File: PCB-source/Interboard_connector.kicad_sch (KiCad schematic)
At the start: 1 part, among them J1 86093488324755V1LF

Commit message: ch32
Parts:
- added J4: Conn_01x16_Socket, Connector_PinSocket_2.54mm:PinSocket_1x16_P2.54mm_Vertical, symbol Connector:Conn_01x16_Socket
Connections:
- net Chainbus.MISO: now also J1.B11; no longer J1.A11
- net Chainbus.MOSI: now also J1.B12; no longer J1.A12
- net Chainbus.RX: now also J1.B6; no longer J1.A6
- net Chainbus.SCK: now also J1.B13; no longer J1.A13
- net Chainbus.SCL: now also J1.B2; no longer J1.A2
- net Chainbus.SDA: now also J1.B1; no longer J1.A1
- net Chainbus.TX: now also J1.B7; no longer J1.A7
- net Chainbus_I2C_addr0: now also J1.B3; no longer J1.A3
- net Chainbus_I2C_addr1: now also J1.B4; no longer J1.A4
- net Chainbus_I2C_addr2: now also J1.B5; no longer J1.A5
- net Chainbus_SPI_CS0: now also J1.B14; no longer J1.A14
- net Chainbus_SPI_CS1: now also J1.B15; no longer J1.A15
- net Chainbus_SPI_CS2: now also J1.B16; no longer J1.A16
- net Chainbus_UART_addr0: now also J1.B8; no longer J1.A8
- net Chainbus_UART_addr1: now also J1.B9; no longer J1.A9
- net Chainbus_UART_addr2: now also J1.B10; no longer J1.A10
- net GND: now also J1.A14, J1.A6, J1.A7, J1.A8, J1.A9, J4.14 (Pin_14), J4.6 (Pin_6), J4.7 (Pin_7), J4.8 (Pin_8), J4.9 (Pin_9); no longer J1.B10, J1.B13, J1.B14, J1.B15, J1.B16, J1.B7, J1.B8, J1.B9
- new net +3V3: J1.A16, J4.16 (Pin_16)
- new net +5V: J1.A15, J4.15 (Pin_15)
- new net BRD_VIN: J1.A10, J1.A11, J1.A12, J1.A13, J4.10 (Pin_10), J4.11 (Pin_11), J4.12 (Pin_12), J4.13 (Pin_13)
- no-connect marks 0 -> 10
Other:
- moved on the sheet: J1

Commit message: Component placement done
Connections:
- net Altmode10: now also J1.C15; no longer J1.C10
- net Altmode11: now also J1.C7; no longer J1.C11
- net Altmode12: now also J1.C8; no longer J1.C12
- net Altmode13: now also J1.C9; no longer J1.C13
- net Altmode14: now also J1.C10; no longer J1.C14
- net Altmode15: now also J1.C11; no longer J1.C15
- net Altmode7: now also J1.C12; no longer J1.C7
- net Altmode8: now also J1.C13; no longer J1.C8
- net Altmode9: now also J1.C14; no longer J1.C9

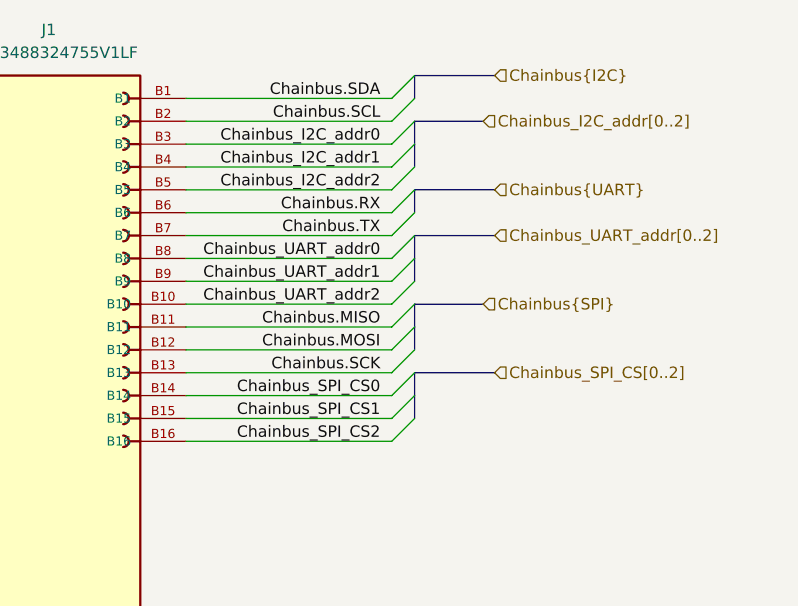
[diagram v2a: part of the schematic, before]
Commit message: processor connection done
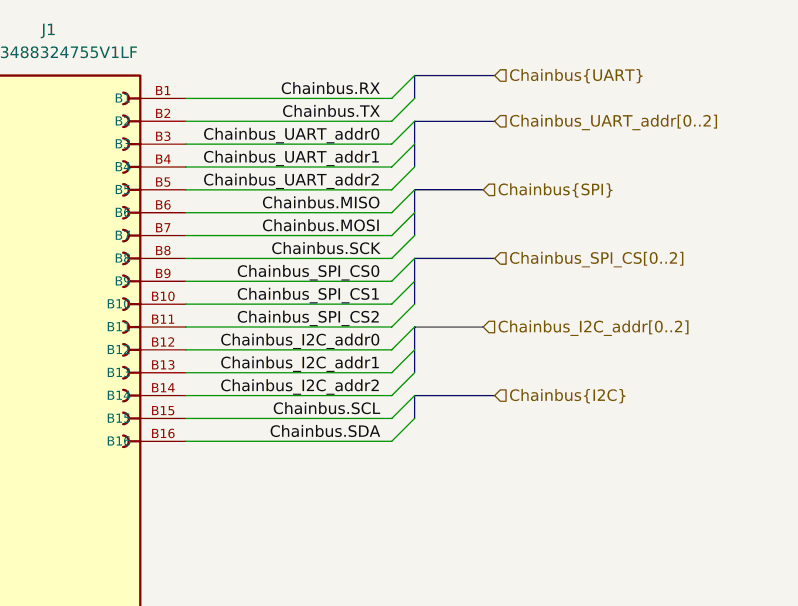
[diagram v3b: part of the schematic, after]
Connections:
- net Chainbus.MISO: now also J1.B6; no longer J1.B11
- net Chainbus.MOSI: now also J1.B7; no longer J1.B12
- net Chainbus.RX: now also J1.B1; no longer J1.B6
- net Chainbus.SCK: now also J1.B8; no longer J1.B13
- net Chainbus.SCL: now also J1.B15; no longer J1.B2
- net Chainbus.SDA: now also J1.B16; no longer J1.B1
- net Chainbus.TX: now also J1.B2; no longer J1.B7
- net Chainbus_I2C_addr0: now also J1.B12; no longer J1.B3
- net Chainbus_I2C_addr1: now also J1.B13; no longer J1.B4
- net Chainbus_I2C_addr2: now also J1.B14; no longer J1.B5
- net Chainbus_SPI_CS0: now also J1.B9; no longer J1.B14
- net Chainbus_SPI_CS1: now also J1.B10; no longer J1.B15
- net Chainbus_SPI_CS2: now also J1.B11; no longer J1.B16
- net Chainbus_UART_addr0: now also J1.B3; no longer J1.B8
- net Chainbus_UART_addr1: now also J1.B4; no longer J1.B9
- net Chainbus_UART_addr2: now also J1.B5; no longer J1.B10

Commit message: silk job, signal ratnest done
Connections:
- net Chainbus_I2C_addr0: now also J1.B9; no longer J1.B12
- net Chainbus_I2C_addr1: now also J1.B10; no longer J1.B13
- net Chainbus_I2C_addr2: now also J1.B11; no longer J1.B14
- net Chainbus_SPI_CS0: now also J1.B12; no longer J1.B9
- net Chainbus_SPI_CS1: now also J1.B13; no longer J1.B10
- net Chainbus_SPI_CS2: now also J1.B14; no longer J1.B11

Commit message: bom done
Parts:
- J1: LCSC (none) -> C5173373
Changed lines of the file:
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@@
+			)
+		)
+		(property "LCSC" "C5173373"
+			(at 148.59 95.25 0)
+			(effects
+				(font
+					(size 1.27 1.27)
+				)
+				(hide yes)
 			)
 		)
